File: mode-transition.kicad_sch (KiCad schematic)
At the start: 21 parts, among them Q19001 DNLS350E, U19001 4069, U19002 4081, U19003 4081, U19004 4073, U19005 4073, U19006 4075, U19007 4075, U19008 4071

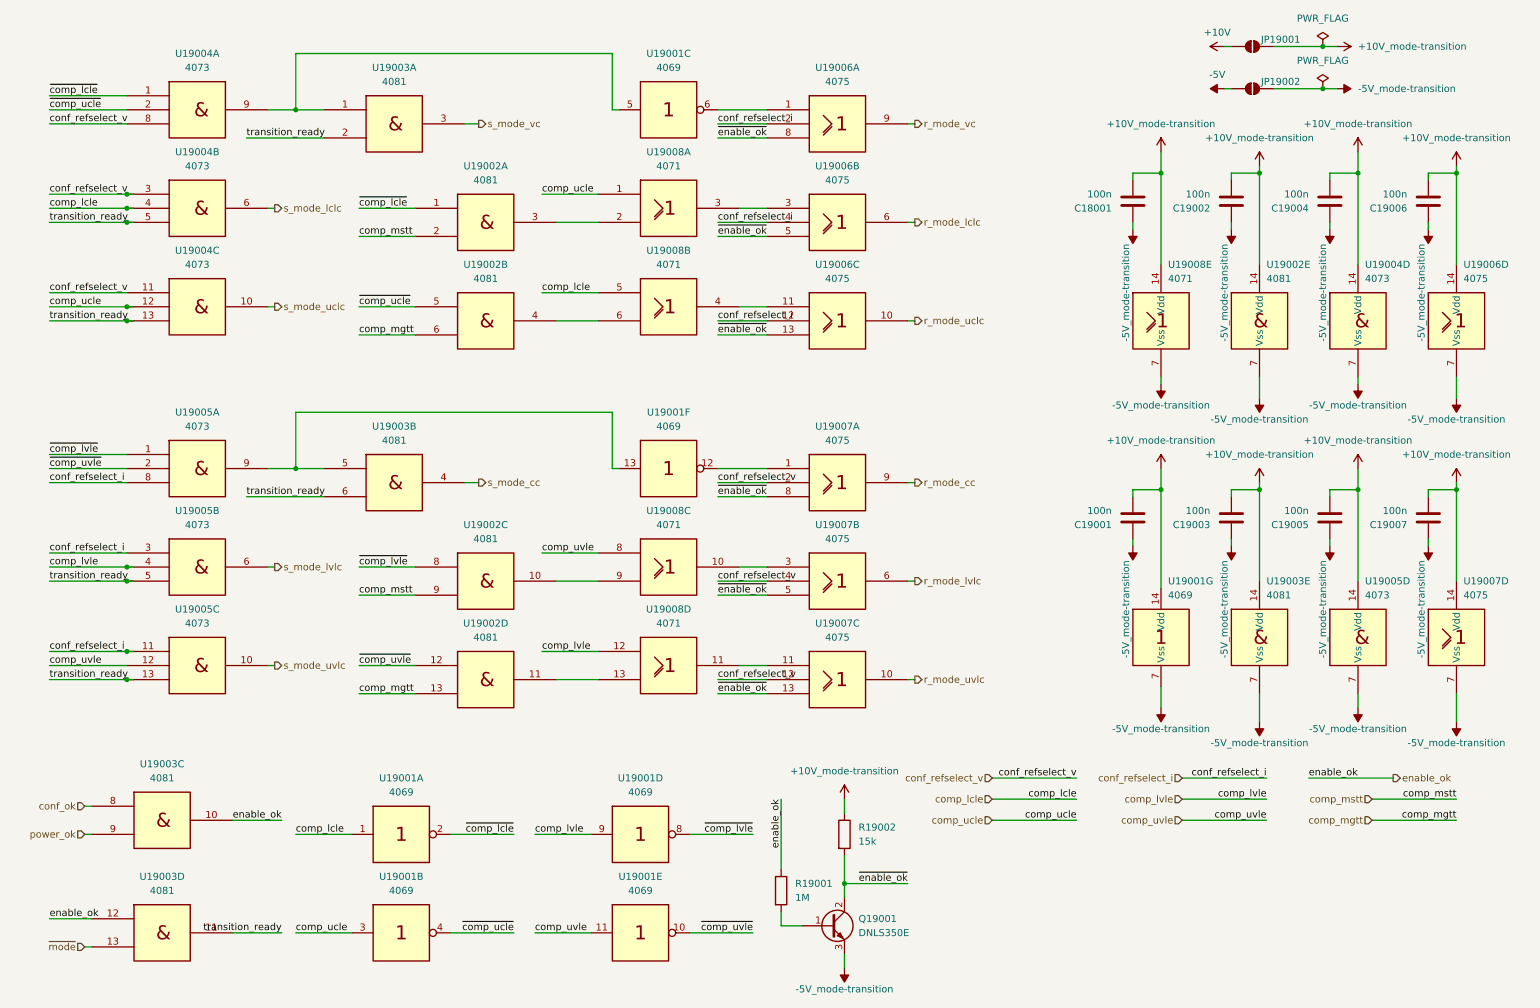
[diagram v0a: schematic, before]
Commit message: add pss 3dmodels and testpoints
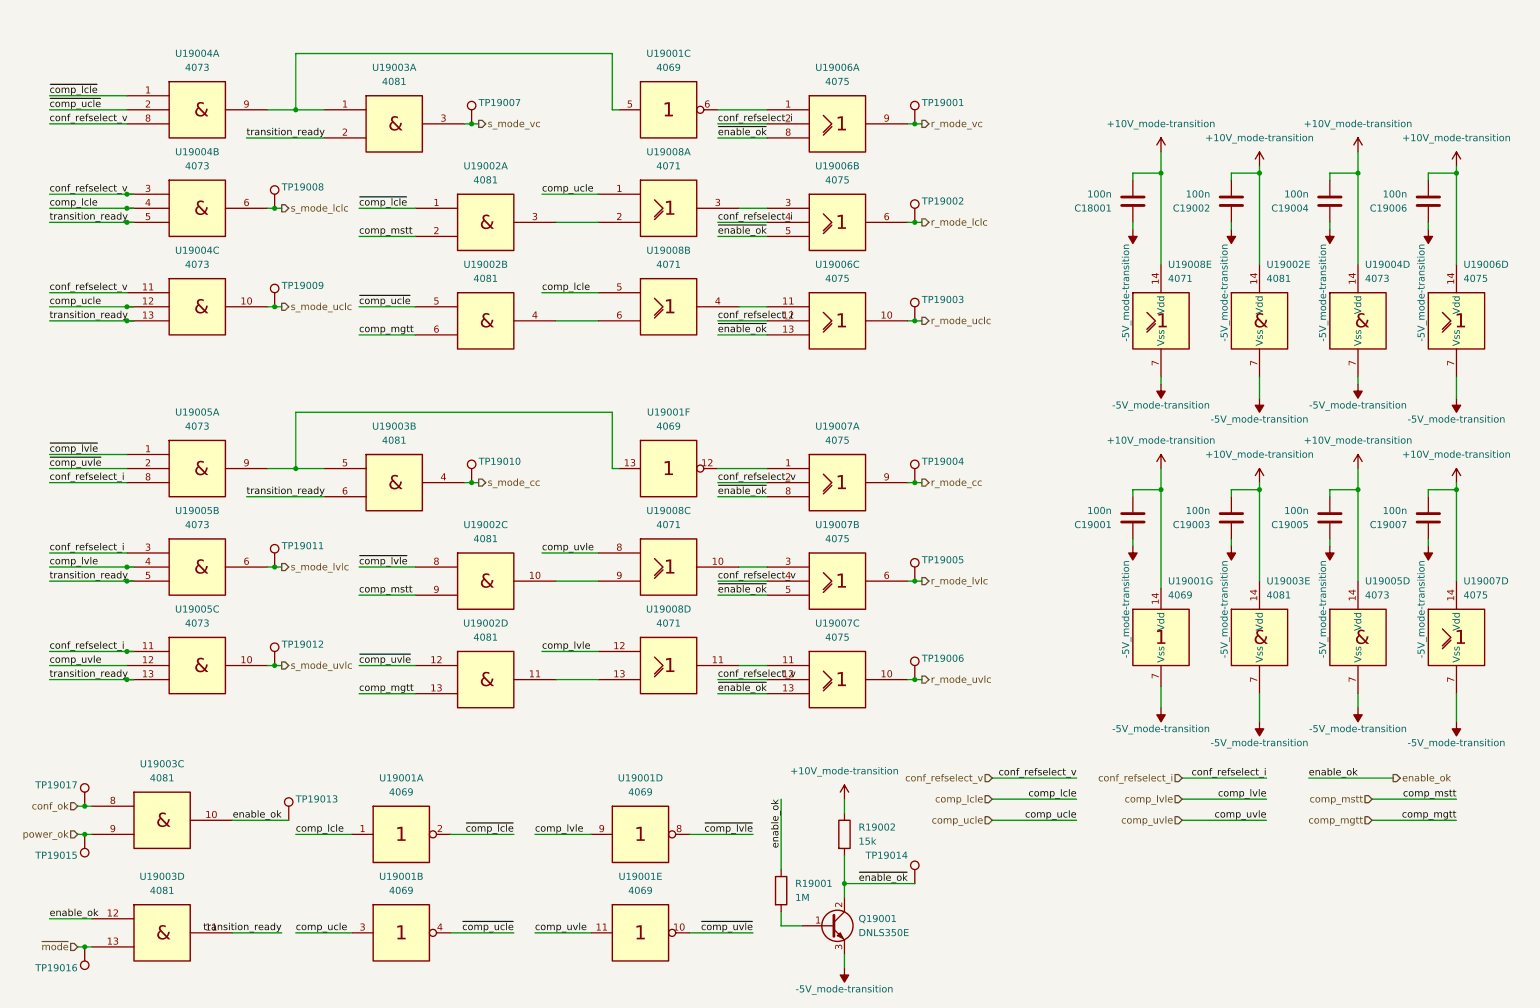
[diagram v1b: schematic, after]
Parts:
- removed JP19001, JP19002: SolderJumper_2_Open, symbol Jumper:SolderJumper_2_Open
- added TP19001, TP19002, TP19003, TP19004, TP19005, TP19006, TP19007, TP19008, TP19009, TP19010, TP19011, TP19012, TP19013, TP19014, TP19015, TP19016, TP19017: ~, pss:TP_0805_2012Metric, symbol Connector:TestPoint
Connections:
- net conf_ok: now also TP19017.1
- net enable_ok: now also TP19013.1
- net power_ok: now also TP19015.1
- net r_mode_cc: now also TP19004.1
- net r_mode_lclc: now also TP19002.1
- net r_mode_lvlc: now also TP19005.1
- net r_mode_uclc: now also TP19003.1
- net r_mode_uvlc: now also TP19006.1
- net r_mode_vc: now also TP19001.1
- net s_mode_cc: now also TP19010.1
- net s_mode_lclc: now also TP19008.1
- net s_mode_lvlc: now also TP19011.1
- net s_mode_uclc: now also TP19009.1
- net s_mode_uvlc: now also TP19012.1
- net s_mode_vc: now also TP19007.1
- net ~{enable_ok}: now also TP19014.1
- net ~{mode}: now also TP19016.1

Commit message: edit pss symbol library: export all schematic symbols to library 'pss' and update symbol link
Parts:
- TP19001, TP19002, TP19003, TP19004, TP19005, TP19006, TP19007, TP19008, TP19009, TP19010, TP19011, TP19012, TP19013, TP19014, TP19015, TP19016, TP19017: symbol Connector:TestPoint -> pss:TestPoint
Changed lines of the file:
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@@
 	)
 	(symbol
-		(lib_id "Connector:TestPoint")
+		(lib_id "pss:TestPoint")
 		(at 59.69 67.31 0)
 		(unit 1)
@@
 	)
 	(symbol
-		(lib_id "Connector:TestPoint")
+		(lib_id "pss:TestPoint")
 		(at 175.26 34.29 0)
 		(unit 1)
@@
 	)
 	(symbol
-		(lib_id "Connector:TestPoint")
+		(lib_id "pss:TestPoint")
 		(at 175.26 52.07 0)
 		(unit 1)
@@
 	)
 	(symbol
-		(lib_id "Connector:TestPoint")
+		(lib_id "pss:TestPoint")
 		(at 175.26 99.06 0)
 		(unit 1)
@@
 	)
 	(symbol
-		(lib_id "Connector:TestPoint")
+		(lib_id "pss:TestPoint")
 		(at 25.4 162.56 180)
 		(unit 1)
@@
 	)
 	(symbol
-		(lib_id "Connector:TestPoint")
+		(lib_id "pss:TestPoint")
 		(at 175.26 116.84 0)
 		(unit 1)
@@
 	)
 	(symbol
-		(lib_id "Connector:TestPoint")
+		(lib_id "pss:TestPoint")
 		(at 25.4 182.88 180)
 		(unit 1)
@@
 	)
 	(symbol
-		(lib_id "Connector:TestPoint")
+		(lib_id "pss:TestPoint")
 		(at 95.25 99.06 0)
 		(unit 1)
@@
 	)
 	(symbol
-		(lib_id "Connector:TestPoint")
+		(lib_id "pss:TestPoint")
 		(at 62.23 160.02 0)
 		(unit 1)
@@
 	)
 	(symbol
-		(lib_id "Connector:TestPoint")
+		(lib_id "pss:TestPoint")
 		(at 175.26 69.85 0)
 		(unit 1)
@@
 	)
 	(symbol
-		(lib_id "Connector:TestPoint")
+		(lib_id "pss:TestPoint")
 		(at 59.69 49.53 0)
 		(unit 1)
@@
 	)
 	(symbol
-		(lib_id "Connector:TestPoint")
+		(lib_id "pss:TestPoint")
 		(at 175.26 171.45 0)
 		(unit 1)
@@
 	)
 	(symbol
-		(lib_id "Connector:TestPoint")
+		(lib_id "pss:TestPoint")
 		(at 59.69 114.3 0)
 		(unit 1)
@@
 	)
 	(symbol
-		(lib_id "Connector:TestPoint")
+		(lib_id "pss:TestPoint")
 		(at 59.69 132.08 0)
 		(unit 1)
@@
 	)
 	(symbol
-		(lib_id "Connector:TestPoint")
+		(lib_id "pss:TestPoint")
 		(at 95.25 34.29 0)
 		(unit 1)
@@
 	)
 	(symbol
-		(lib_id "Connector:TestPoint")
+		(lib_id "pss:TestPoint")
 		(at 25.4 157.48 0)
 		(mirror y)
@@
 	)
 	(symbol
-		(lib_id "Connector:TestPoint")
+		(lib_id "pss:TestPoint")
 		(at 175.26 134.62 0)
 		(unit 1)

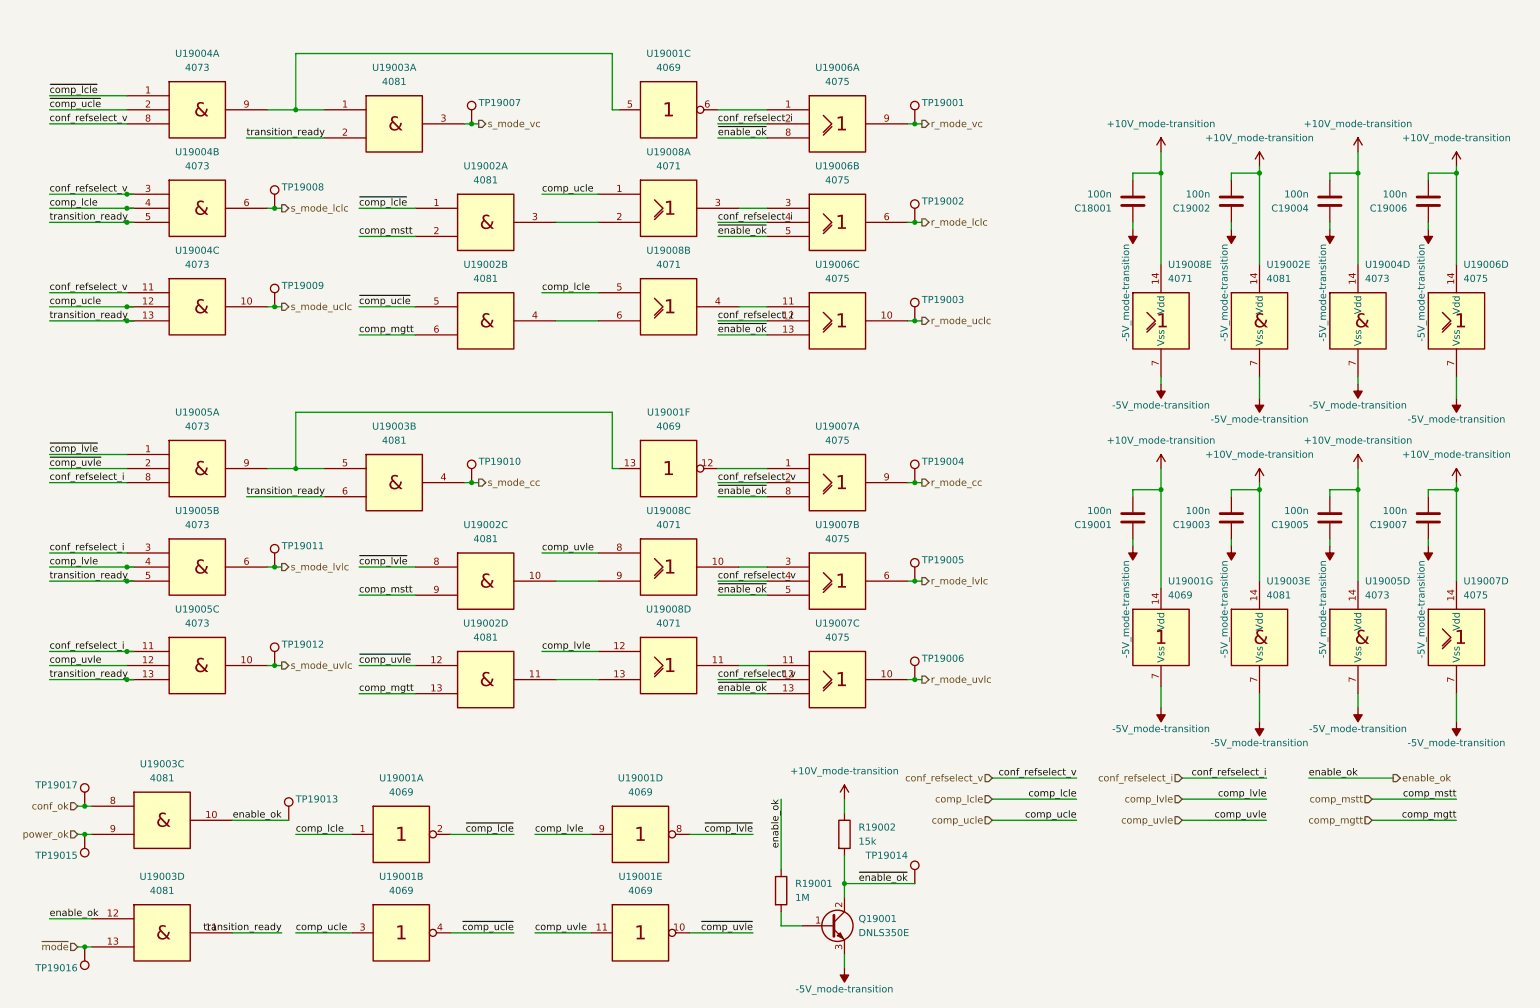
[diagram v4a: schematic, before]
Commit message: edit pss footprint library: export all footprints to library 'pss' and update footprint links
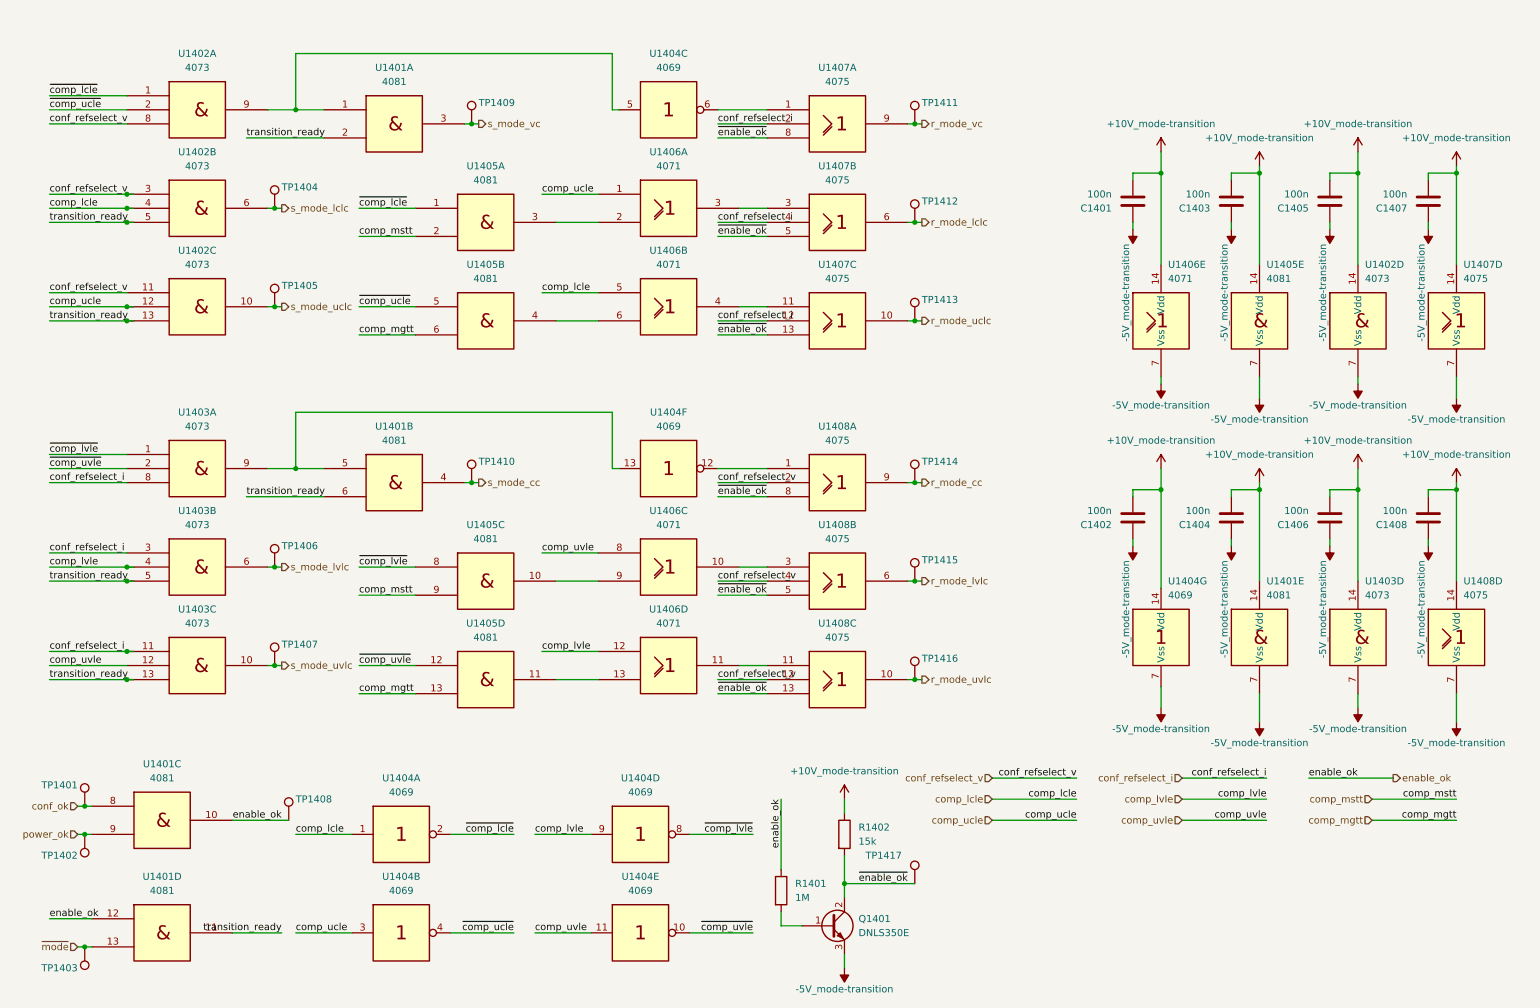
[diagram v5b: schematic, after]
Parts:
- C1401: renamed from C18001; footprint Capacitor_SMD:C_0805_2012Metric_Pad1.18x1.45mm_HandSolder -> pss:C_0805_2012Metric_Pad1.18x1.45mm_HandSolder
- C1402: renamed from C19001; footprint Capacitor_SMD:C_0805_2012Metric_Pad1.18x1.45mm_HandSolder -> pss:C_0805_2012Metric_Pad1.18x1.45mm_HandSolder
- C1403: renamed from C19002; footprint Capacitor_SMD:C_0805_2012Metric_Pad1.18x1.45mm_HandSolder -> pss:C_0805_2012Metric_Pad1.18x1.45mm_HandSolder
- C1404: renamed from C19003; footprint Capacitor_SMD:C_0805_2012Metric_Pad1.18x1.45mm_HandSolder -> pss:C_0805_2012Metric_Pad1.18x1.45mm_HandSolder
- C1405: renamed from C19004; footprint Capacitor_SMD:C_0805_2012Metric_Pad1.18x1.45mm_HandSolder -> pss:C_0805_2012Metric_Pad1.18x1.45mm_HandSolder
- C1406: renamed from C19005; footprint Capacitor_SMD:C_0805_2012Metric_Pad1.18x1.45mm_HandSolder -> pss:C_0805_2012Metric_Pad1.18x1.45mm_HandSolder
- C1407: renamed from C19006; footprint Capacitor_SMD:C_0805_2012Metric_Pad1.18x1.45mm_HandSolder -> pss:C_0805_2012Metric_Pad1.18x1.45mm_HandSolder
- C1408: renamed from C19007; footprint Capacitor_SMD:C_0805_2012Metric_Pad1.18x1.45mm_HandSolder -> pss:C_0805_2012Metric_Pad1.18x1.45mm_HandSolder
- Q1401: renamed from Q19001; footprint Package_TO_SOT_SMD:SOT-223-3_TabPin2 -> pss:SOT-223-3_TabPin2
- R1401: renamed from R19001; footprint Resistor_SMD:R_1210_3225Metric_Pad1.30x2.65mm_HandSolder -> pss:R_1210_3225Metric_Pad1.30x2.65mm_HandSolder
- R1402: renamed from R19002; footprint Resistor_SMD:R_1210_3225Metric_Pad1.30x2.65mm_HandSolder -> pss:R_1210_3225Metric_Pad1.30x2.65mm_HandSolder
- U1401: renamed from U19003; footprint Package_SO:SOIC-14_3.9x8.7mm_P1.27mm -> pss:SOIC-14_3.9x8.7mm_P1.27mm
- U1402: renamed from U19004; footprint Package_SO:SOIC-14_3.9x8.7mm_P1.27mm -> pss:SOIC-14_3.9x8.7mm_P1.27mm
- U1403: renamed from U19005; footprint Package_SO:SOIC-14_3.9x8.7mm_P1.27mm -> pss:SOIC-14_3.9x8.7mm_P1.27mm
- U1404: renamed from U19001; footprint Package_SO:SOIC-14_3.9x8.7mm_P1.27mm -> pss:SOIC-14_3.9x8.7mm_P1.27mm
- U1405: renamed from U19002; footprint Package_SO:SOIC-14_3.9x8.7mm_P1.27mm -> pss:SOIC-14_3.9x8.7mm_P1.27mm
- U1406: renamed from U19008; footprint Package_SO:SOIC-14_3.9x8.7mm_P1.27mm -> pss:SOIC-14_3.9x8.7mm_P1.27mm
- U1407: renamed from U19006; footprint Package_SO:SOIC-14_3.9x8.7mm_P1.27mm -> pss:SOIC-14_3.9x8.7mm_P1.27mm
- U1408: renamed from U19007; footprint Package_SO:SOIC-14_3.9x8.7mm_P1.27mm -> pss:SOIC-14_3.9x8.7mm_P1.27mm
- renumbered TP19017 to TP1401, TP19015 to TP1402, TP19016 to TP1403, TP19008 to TP1404, TP19009 to TP1405, TP19011 to TP1406, TP19012 to TP1407, TP19013 to TP1408, TP19007 to TP1409, TP19010 to TP1410, TP19001 to TP1411, TP19002 to TP1412, TP19003 to TP1413, TP19004 to TP1414, TP19005 to TP1415, TP19006 to TP1416, TP19014 to TP1417
